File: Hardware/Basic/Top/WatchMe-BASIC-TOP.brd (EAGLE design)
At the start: 38 x 38 mm, 62 parts, among them SW1 SWITCH.MOM, SW2 SWITCH.MOM, U2 NRF52832_MODULE_MDBT42, U4 PCF8523, U5 FT231XS

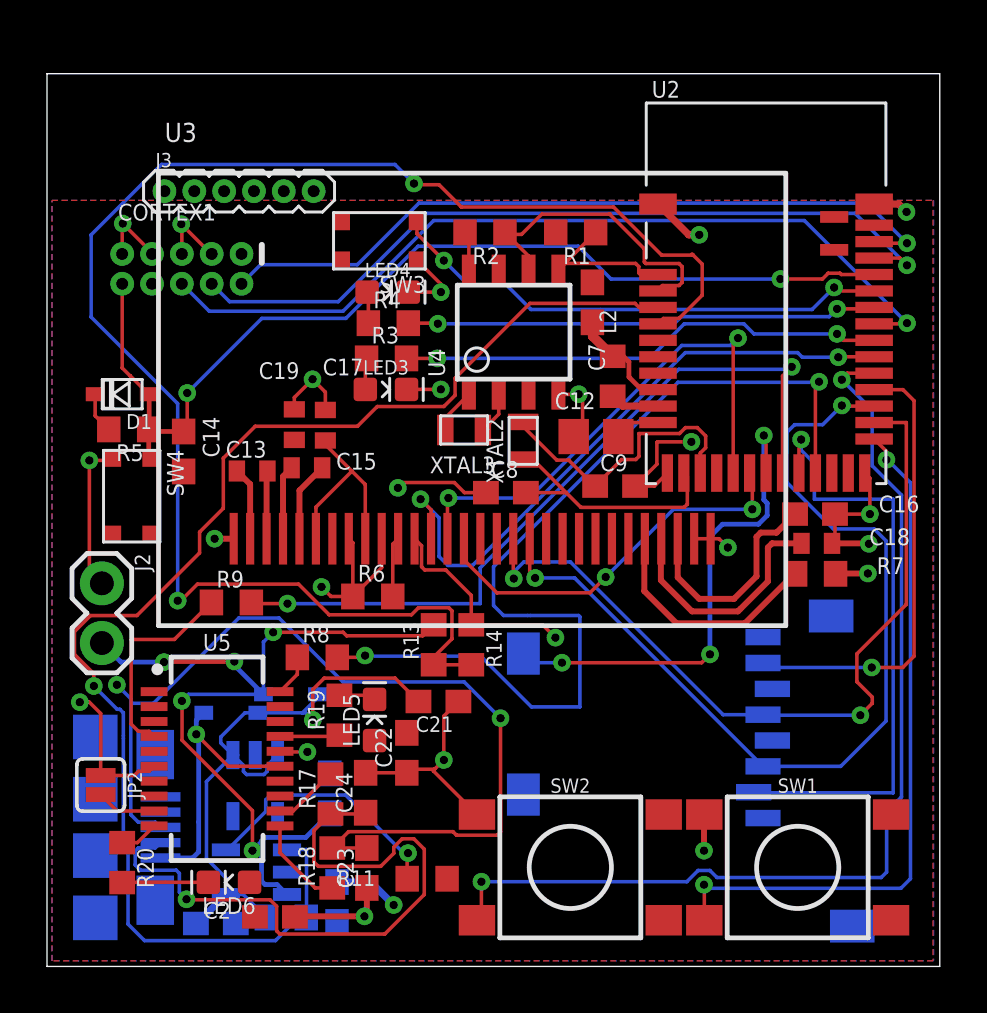
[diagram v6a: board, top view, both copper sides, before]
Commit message: fixed all DRC errors/warnings
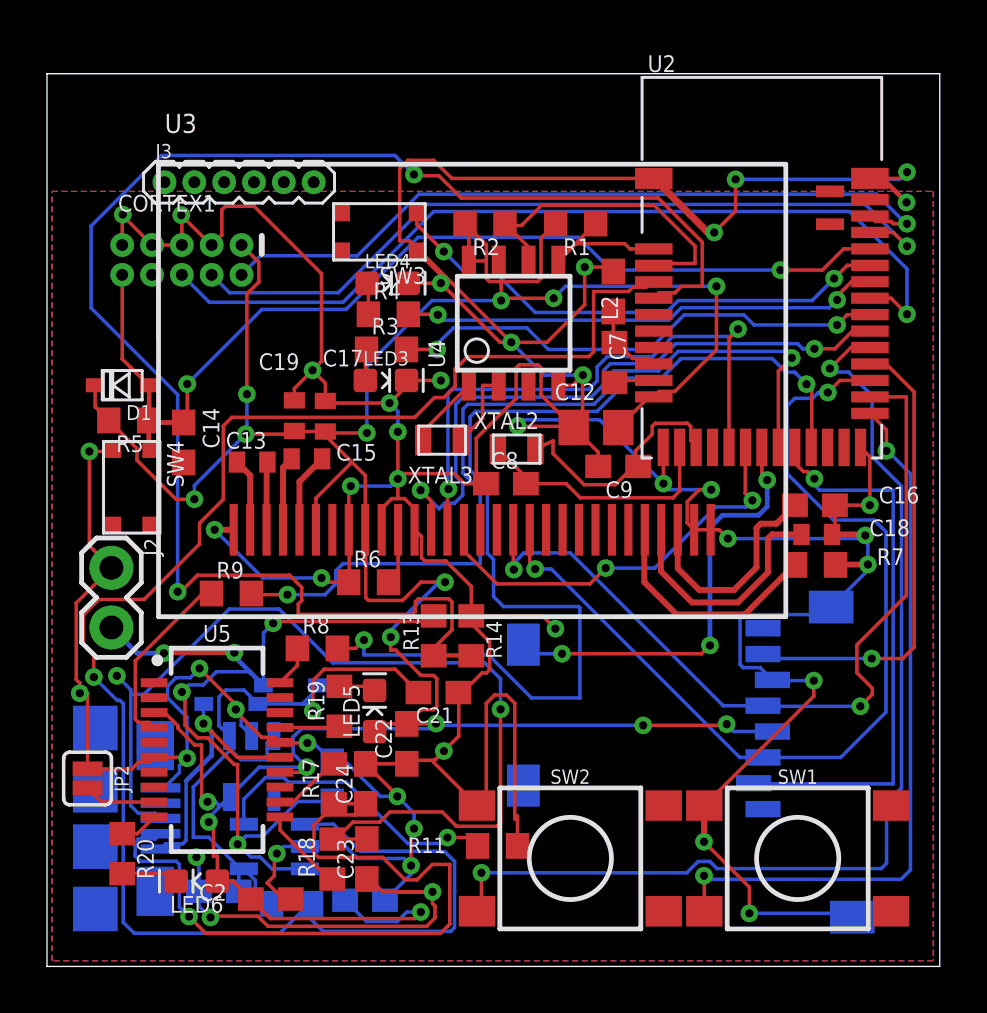
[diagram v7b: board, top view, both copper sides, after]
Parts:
- moved R11 3.31 mm to (19.2, 5.13)
- moved C5 1.38 mm to (7.32, 3.20), turned to 180 degrees
- moved LED6 1.37 mm to (6.38, 3.63)
- moved CHRG2 1.33 mm to (9.68, 5.11)
- moved C6 1.20 mm to (13.5, 2.82), turned to 180 degrees
- moved U2 1.11 mm to (30.4, 29.7)
- moved XTAL3 1.03 mm to (16.8, 22.4)
- moved C7 1.00 mm to (24.1, 28.7)
- moved C9 0.85 mm to (24.3, 21.3), turned to 180 degrees
- moved LDO2 0.83 mm to (8.71, 8.51)
- moved C2 0.78 mm to (9.53, 2.87)
- moved J2 0.78 mm to (2.74, 17.0)
- moved R6 0.64 mm to (13.7, 16.4)
- moved R12 0.63 mm to (10.4, 2.67)
- moved JP2 0.62 mm to (1.73, 8.00)
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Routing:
- net GND: track 86.4 -> 296.9 mm, vias 23 -> 43
- net 3.3V: track 16.6 -> 141.1 mm, vias 1 -> 16
- net D27/CHRG.STATUS: track 58.5 -> 74.1 mm
- net RXD.NRF: track 41.7 -> 46.5 mm
- net TXD.NRF: track 32.8 -> 37.0 mm
- net USB-: track 28.5 -> 32.0 mm
- net D5/CD1: track 21.2 -> 18.7 mm
- net D3/RESET.OLED: track 22.7 -> 24.9 mm
- net D7/SD.CS: track 26.0 -> 23.9 mm
- net N$6: track 12.4 -> 10.6 mm
- net N$17: track 11.1 -> 12.8 mm
- net N$19: track 1.79 -> 3.39 mm
- net SWO: track 36.2 -> 37.7 mm
- net A4/BATT: track 66.8 -> 68.3 mm
- net VLIPO: track 36.0 -> 37.6 mm
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
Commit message: fixed remaining warnings
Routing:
- net VLIPO: track 37.6 -> 36.5 mm
- net GND: track 296.9 -> 296.1 mm
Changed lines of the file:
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@@
 <wire x1="14.247" y1="18.5866" x2="14.2386" y2="18.595" width="0.1524" layer="1"/>
 <wire x1="14.2386" y1="19.4764875" x2="14.2386" y2="18.595" width="0.1524" layer="1"/>
-<wire x1="8.7122" y1="9.8091" x2="8.7122" y2="10.30668125" width="0.1524" layer="16"/>
 <wire x1="14.8844" y1="19.9152" x2="14.9352" y2="19.966" width="0.1524" layer="1"/>
 <wire x1="14.9352" y1="19.966" x2="14.9352" y2="20.7518" width="0.1524" layer="1"/>
@@
 <wire x1="12.7047" y1="5.1054" x2="10.9775" y2="5.1054" width="0.1524" layer="16"/>
 <wire x1="15.1892" y1="4.5974" x2="13.2127" y2="4.5974" width="0.1524" layer="16"/>
-<wire x1="10.9775" y1="5.1054" x2="10.7743" y2="4.9022" width="0.1524" layer="16"/>
 <wire x1="9.6774" y1="4.699" x2="9.78376875" y2="4.80536875" width="0.1524" layer="1"/>
 <via x="9.78376875" y="4.80536875" extent="1-16" drill="0.35"/>
@@
 <contactref element="C20" pad="1"/>
 <contactref element="R13" pad="2"/>
-<wire x1="12.1412" y1="7.024" x2="11.9966" y2="7.1686" width="0.2032" layer="16"/>
 <wire x1="9.2132" y1="11.9634" x2="9.2132" y2="14.1916" width="0.1524" layer="16"/>
 <wire x1="9.2132" y1="14.1916" x2="9.6266" y2="14.605" width="0.1524" layer="16"/>
@@
 <wire x1="9.6266" y1="14.605" x2="9.7028" y2="14.6812" width="0.1524" layer="1"/>
 <wire x1="16.2188" y1="14.6812" x2="16.4592" y2="14.9216" width="0.1524" layer="1"/>
-<via x="5.7404" y="11.684" extent="1-16" drill="0.35"/>
 <wire x1="5.8751" y1="11.5493" x2="5.7404" y2="11.684" width="0.1524" layer="1"/>
 <wire x1="5.8751" y1="10.26425" x2="5.8751" y2="11.5493" width="0.1524" layer="1"/>
-<wire x1="5.7404" y1="11.684" x2="6.0198" y2="11.9634" width="0.1524" layer="16"/>
 <wire x1="9.2132" y1="11.9634" x2="8.6325" y2="12.5441" width="0.2032" layer="16"/>
 <wire x1="8.6325" y1="12.5441" x2="7.9756" y2="13.201" width="0.2032" layer="16"/>
@@
 <via x="8.11565" y="5.199" extent="1-16" drill="0.35"/>
 <wire x1="8.11565" y1="5.199" x2="8.11565" y2="8.5979" width="0.1524" layer="1"/>
-<wire x1="8.125825" y1="5.209175" x2="8.43425" y2="5.5176" width="0.1524" layer="16"/>
 <wire x1="8.125825" y1="5.209175" x2="8.11565" y2="5.199" width="0.1524" layer="16"/>
 <wire x1="9.0719875" y1="4.659" x2="8.676" y2="4.659" width="0.1524" layer="16"/>
@@
 <wire x1="10.9775" y1="4.1554" x2="9.5755875" y2="4.1554" width="0.1524" layer="16"/>
 <wire x1="9.5755875" y1="4.1554" x2="9.0719875" y2="4.659" width="0.1524" layer="16"/>
-<wire x1="8.11565" y1="5.199" x2="8.46845" y2="5.5518" width="0.1524" layer="16"/>
-<wire x1="8.46845" y1="5.5518" x2="9.2033875" y2="5.5518" width="0.1524" layer="16"/>
-<wire x1="9.2033875" y1="5.5518" x2="10.6755875" y2="7.024" width="0.1524" layer="16"/>
+<wire x1="8.11565" y1="5.199" x2="8.19185" y2="5.199" width="0.1524" layer="16"/>
+<wire x1="8.51925" y1="5.5264" x2="8.19185" y2="5.199" width="0.1524" layer="16"/>
+<wire x1="8.51925" y1="5.5264" x2="9.1779875" y2="5.5264" width="0.1524" layer="16"/>
+<wire x1="9.1779875" y1="5.5264" x2="10.6755875" y2="7.024" width="0.1524" layer="16"/>
 <wire x1="10.6755875" y1="7.024" x2="12.1412" y2="7.024" width="0.1524" layer="16"/>
-<wire x1="5.7404" y1="11.684" x2="6.0424" y2="11.986" width="0.1524" layer="16"/>
 <wire x1="7.21218125" y1="12.5441" x2="8.6325" y2="12.5441" width="0.1524" layer="16"/>
 <wire x1="6.0424" y1="11.986" x2="6.65408125" y2="11.986" width="0.1524" layer="16"/>
 <wire x1="6.65408125" y1="11.986" x2="7.21218125" y2="12.5441" width="0.1524" layer="16"/>
+<via x="5.7404" y="11.684" extent="1-16" drill="0.35"/>
+<wire x1="5.7404" y1="11.684" x2="6.0424" y2="11.986" width="0.1524" layer="16"/>
 </signal>
 <signal name="V_USB">
